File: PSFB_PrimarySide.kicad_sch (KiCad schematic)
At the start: 15 parts

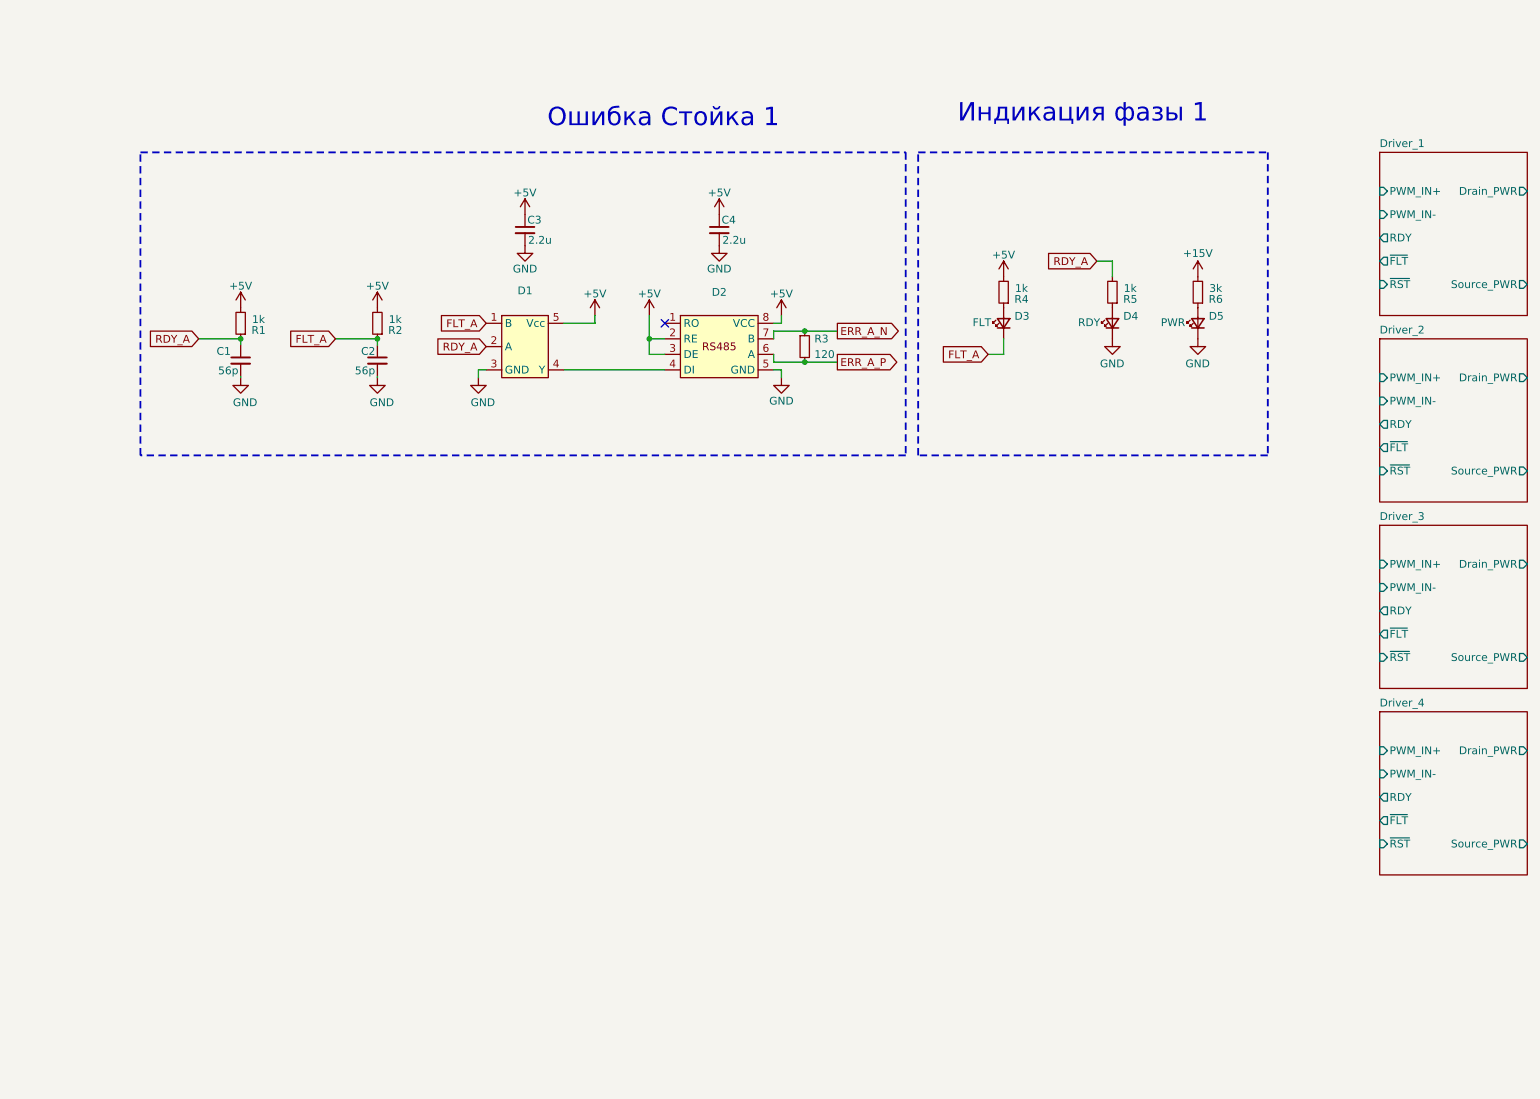
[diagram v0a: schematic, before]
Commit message: VER1.0: развел 4 канала
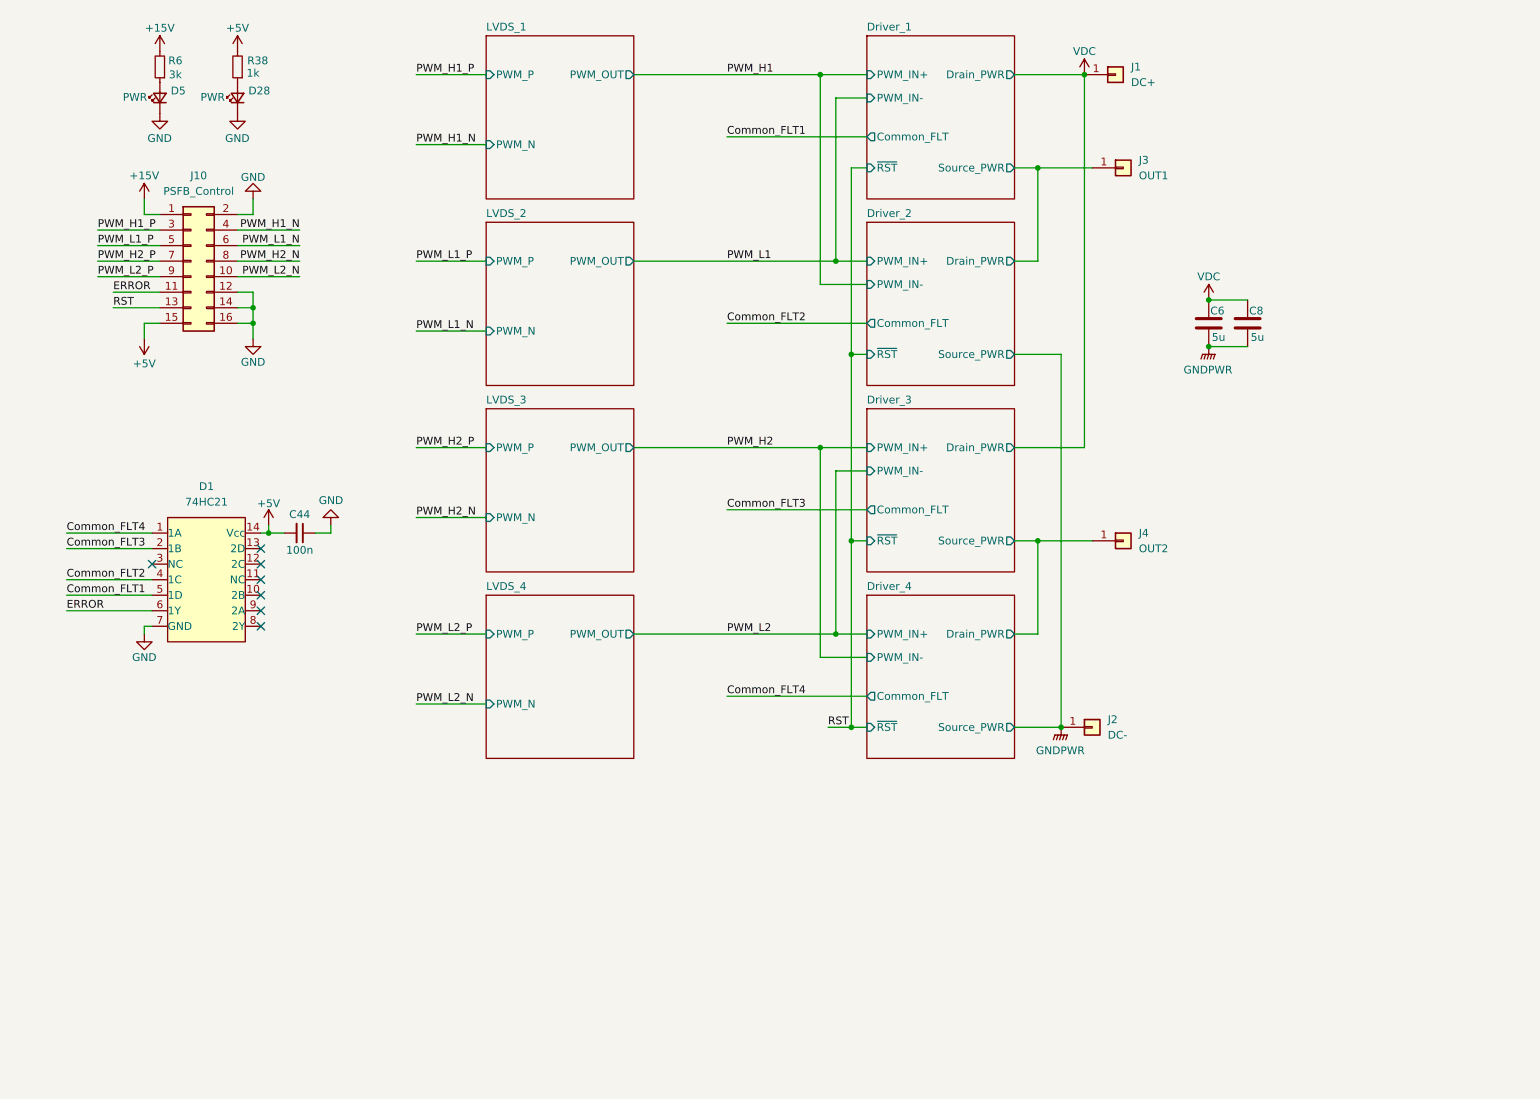
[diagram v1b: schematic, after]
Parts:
- removed C1, C2: 56p, Capacitor_SMD:C_0805_2012Metric_Pad1.18x1.45mm_HandSolder, symbol Device:C_Small
- removed C3, C4: 2.2u, Capacitor_SMD:C_0805_2012Metric_Pad1.18x1.45mm_HandSolder, symbol Device:C_Small
- removed D1: (no value), Package_TO_SOT_SMD:SOT-23-5_HandSoldering, symbol Logic_My:MC74VHC1GT08DTT1G
- removed D2: (no value), Package_SO:SOIC-8_3.9x4.9mm_P1.27mm, symbol Interface_My:ADM3485E_1
- removed D3, D4: (no value), LED_SMD:LED_0805_2012Metric_Pad1.15x1.40mm_HandSolder, symbol Device:LED_Small
- removed R1, R2, R4, R5: 1k, Resistor_SMD:R_0805_2012Metric_Pad1.20x1.40mm_HandSolder, symbol Device:R_Small
- removed R3: 120, Resistor_SMD:R_0805_2012Metric_Pad1.20x1.40mm_HandSolder, symbol Device:R_Small
- added C44: 100n, Capacitor_SMD:C_0805_2012Metric_Pad1.18x1.45mm_HandSolder, symbol Device:C_Small
- added C6, C8: 5u, Capacitor_THT:C_Rect_L31.5mm_W15.0mm_P27.50mm_MKS4, symbol Device:C
- added D1: 74HC21, Package_SO:SOIC-14_3.9x8.7mm_P1.27mm, symbol Logic_my:74HC21
- added D28: (no value), LED_SMD:LED_0805_2012Metric_Pad1.15x1.40mm_HandSolder, symbol Device:LED_Small
- added J1: DC+, symbol Connector_Generic:Conn_01x01
- added J10: PSFB_Control, Connector_IDC:IDC-Header_2x08_P2.54mm_Vertical, symbol Connector_Generic:Conn_02x08_Odd_Even
- added J2: DC-, symbol Connector_Generic:Conn_01x01
- added J3: OUT1, symbol Connector_Generic:Conn_01x01
- added J4: OUT2, symbol Connector_Generic:Conn_01x01
- added R38: 1k, Resistor_SMD:R_0805_2012Metric_Pad1.20x1.40mm_HandSolder, symbol Device:R_Small
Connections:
- net +15V: now also J10.1 (Pin_1)
- net +5V: now also C44.2, D1.14 (Vcc), J10.15 (Pin_15), R38.2
- net Driver_1/Source_PWR: now also J3.1 (Pin_1)
- net Driver_3/Source_PWR: now also J4.1 (Pin_1)
- net GND: now also C44.1, D1.7 (GND), D28.1 (K), J10.12 (Pin_12), J10.14 (Pin_14), J10.16 (Pin_16), J10.2 (Pin_2)
- new net: D28.2 (A), R38.1
- new net Common_FLT1: D1.5 (1D)
- new net Common_FLT2: D1.4 (1C)
- new net Common_FLT3: D1.2 (1B)
- new net Common_FLT4: D1.1 (1A)
- new net ERROR: D1.6 (1Y), J10.11 (Pin_11)
- new net GNDPWR: C6.2, C8.2, J2.1 (Pin_1)
- new net PWM_H1_N: J10.4 (Pin_4)
- new net PWM_H1_P: J10.3 (Pin_3)
- new net PWM_H2_N: J10.8 (Pin_8)
- new net PWM_H2_P: J10.7 (Pin_7)
- new net PWM_L1_N: J10.6 (Pin_6)
- new net PWM_L1_P: J10.5 (Pin_5)
- new net PWM_L2_N: J10.10 (Pin_10)
- new net PWM_L2_P: J10.9 (Pin_9)
- new net RST: J10.13 (Pin_13)
- new net VDC: C6.1, C8.1, J1.1 (Pin_1)
- no-connect marks 1 -> 7
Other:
- added sheet LVDS_1 (LVDS.kicad_sch)
- added sheet LVDS_2 (LVDS.kicad_sch)
- added sheet LVDS_3 (LVDS.kicad_sch)
- added sheet LVDS_4 (LVDS.kicad_sch)
- sheet Driver_1 ports: added Common_FLT; removed RDY, ~{FLT}
- sheet Driver_2 ports: added Common_FLT; removed RDY, ~{FLT}
- sheet Driver_3 ports: added Common_FLT; removed RDY, ~{FLT}
- sheet Driver_4 ports: added Common_FLT; removed RDY, ~{FLT}
- note removed: "Индикация фазы 1"
- note removed: "Ошибка Стойка 1"
- moved on the sheet: D5, R6

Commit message: VER1.0: добавил разъем под FFC
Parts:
- removed J10: PSFB_Control, Connector_IDC:IDC-Header_2x08_P2.54mm_Vertical, symbol Connector_Generic:Conn_02x08_Odd_Even
- added C14, C30: 100n, Capacitor_SMD:C_1812_4532Metric_Pad1.57x3.40mm_HandSolder, symbol Device:C
- added C3: 22u, Capacitor_Tantalum_SMD:CP_EIA-3216-18_Kemet-A_HandSolder, symbol Device:C_Polarized_Small
- added C49: 10u, Capacitor_Tantalum_SMD:CP_EIA-3216-18_Kemet-A_HandSolder, symbol Device:C_Polarized_Small
- added C50: 10u, Capacitor_SMD:C_1206_3216Metric_Pad1.33x1.80mm_HandSolder, symbol Device:C_Small
- added C53: 100n, Capacitor_SMD:C_0805_2012Metric_Pad1.18x1.45mm_HandSolder, symbol Device:C_Small
- added D2: K78xx-500R3, MORNSUN:K78xx-500R3 ÕýÊä³ö, symbol MORNSUN:K78xx-500R3 正输出
- added J10: PSFB_Control, Connector_FFC-FPC:Hirose_FH12-20S-0.5SH_1x20-1MP_P0.50mm_Horizontal, symbol Connector_Generic:Conn_01x20
- added J12, J9: Supply, Connector_PinSocket_2.54mm:PinSocket_2x02_P2.54mm_Vertical, symbol Connector_Generic:Conn_02x02_Odd_Even
- added U5: AMS1117-3.3, Package_TO_SOT_SMD:SOT-223-3_TabPin2, symbol Regulator_Linear:AMS1117-3.3
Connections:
- net +15V: now also C50.1, D2.1 (Vin), J10.1 (Pin_1), J10.2 (Pin_2), J9.2 (Pin_2), J9.4 (Pin_4)
- net +5V: now also C49.1, C53.1, D2.3 (+Vo), U5.3 (VI); no longer C44.2, D1.14 (Vcc), R38.2
- net ERROR: now also J10.6 (Pin_6)
- net GND: now also C3.2, C49.2, C50.2, C53.2, D2.2 (GND), J10.12 (Pin_12), J10.15 (Pin_15), J10.18 (Pin_18), J10.3 (Pin_3), J10.4 (Pin_4), J10.5 (Pin_5), J10.7 (Pin_7), J10.9 (Pin_9), J12.1 (Pin_1), J12.2 (Pin_2), J12.3 (Pin_3), J12.4 (Pin_4), J9.1 (Pin_1), J9.3 (Pin_3), U5.1 (GND)
- net GNDPWR: now also C14.2, C30.2
- net PWM_H1_N: now also J10.11 (Pin_11)
- net PWM_H1_P: now also J10.10 (Pin_10)
- net PWM_H2_N: now also J10.17 (Pin_17)
- net PWM_H2_P: now also J10.16 (Pin_16)
- net PWM_L1_N: now also J10.14 (Pin_14)
- net PWM_L1_P: now also J10.13 (Pin_13)
- net PWM_L2_N: now also J10.20 (Pin_20)
- net PWM_L2_P: now also J10.19 (Pin_19)
- net RST: now also J10.8 (Pin_8)
- net VDC: now also C14.1, C30.1
- new net +3.3V: C3.1, C44.2, D1.14 (Vcc), R38.2, U5.2 (VO)
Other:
- moved on the sheet: D28, D5, R38, R6

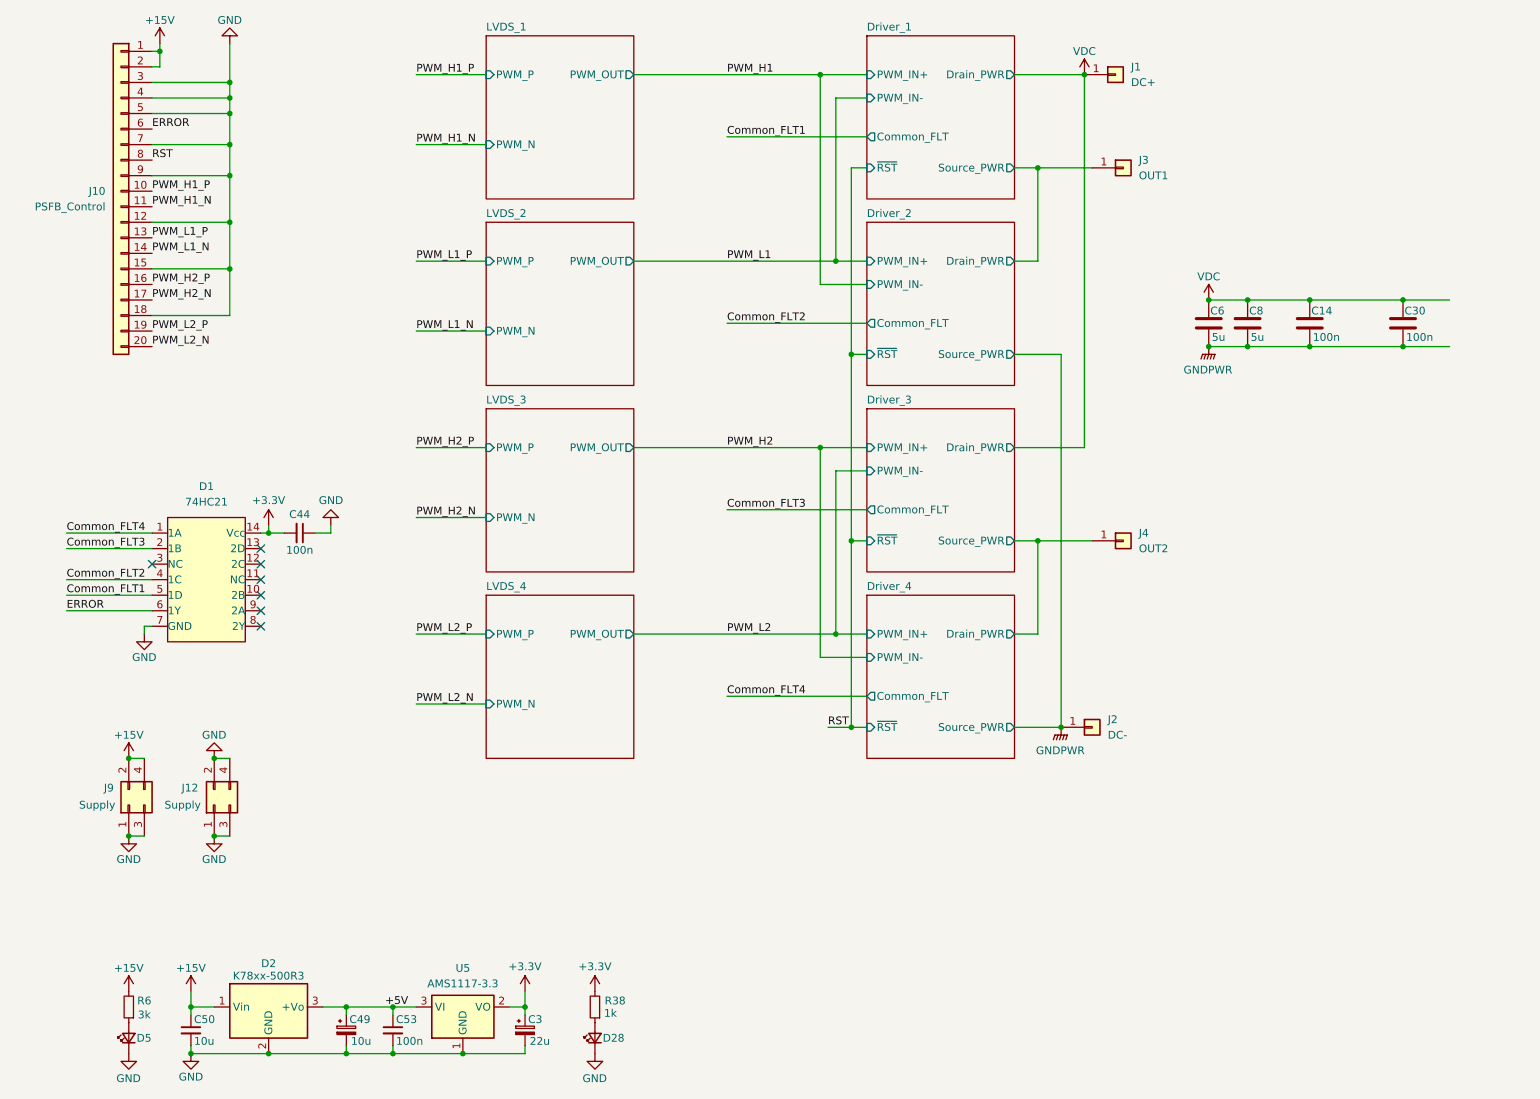
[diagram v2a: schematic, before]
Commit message: VER1.0: добавил плату питания драйверов и развел всю силовую плату
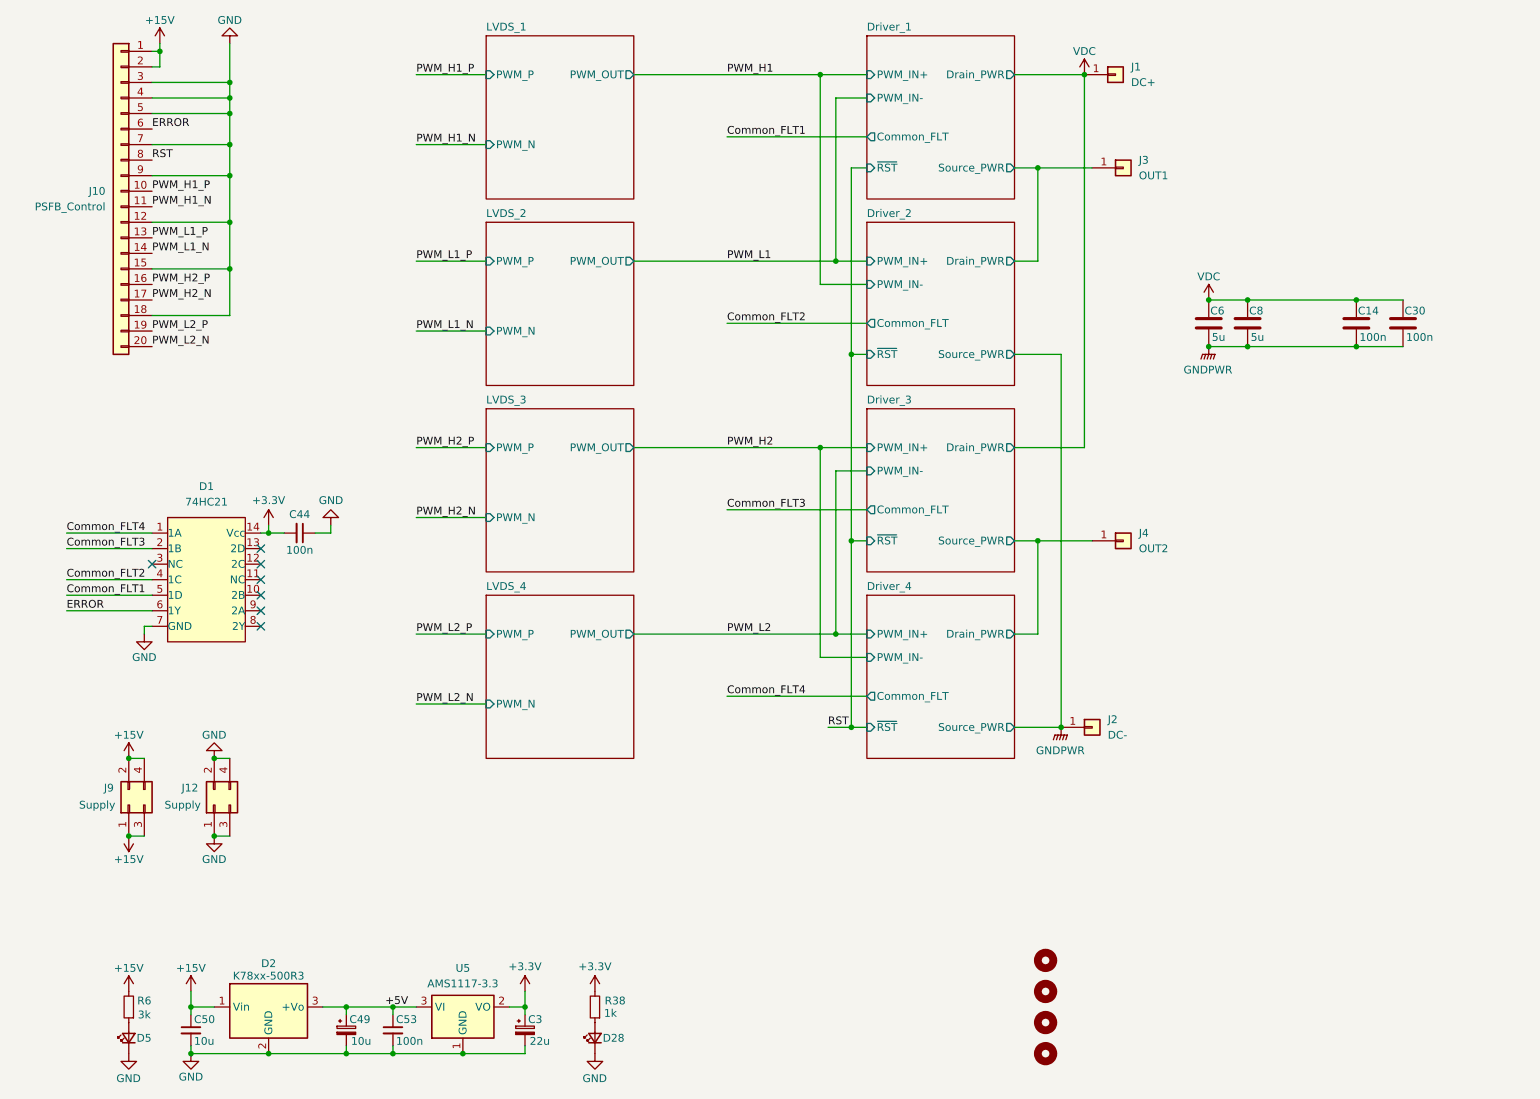
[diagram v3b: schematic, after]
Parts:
- added H1, H2, H3, H4: MountingHole, MountingHole:MountingHole_4.3mm_M4, symbol Mechanical:MountingHole
- J1, J2, J3, J4: footprint (none) -> Connector_my:Bush_1x8
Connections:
- net +15V: now also J9.1 (Pin_1), J9.3 (Pin_3)
- net GND: no longer J9.1 (Pin_1), J9.3 (Pin_3)
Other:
- moved on the sheet: C14

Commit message: VER1.0: добавил ресет общий
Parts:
- added Q5: (no value), Package_TO_SOT_SMD:SOT-23, symbol Device:Q_NPN_BEC
- added R100: 4.7k, Resistor_SMD:R_0805_2012Metric_Pad1.20x1.40mm_HandSolder, symbol Device:R_Small
- added R101: 1k, Resistor_SMD:R_0805_2012Metric_Pad1.20x1.40mm_HandSolder, symbol Device:R_Small
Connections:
- net +3.3V: now also R101.2
- net GND: now also Q5.2 (E)
- net RST: now also R100.1
- new net: Q5.1 (B), R100.2
- new net Driver_1/~{RST}: Q5.3 (C), R101.1

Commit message: VER1.0: сделал файлы для производства
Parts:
- C14, C30: Description P/N (none) -> Capacitor Film; Product Name (none) -> C1812X104K102T
- C3: Description P/N (none) -> Capacitor Tantalum SMD; Product Name (none) -> CA45-A010K226T
- C44, C50, C53: Description P/N Capacitor SMD 25+V -> Capacitor SMD 50V
- C49: Description P/N (none) -> Capacitor Tantalum SMD; Product Name (none) -> CA45-A010K106T
- C6, C8: Description P/N (none) -> Capacitor Film; Product Name (none) -> B32774D8505K000
- D1: value 74HC21 -> (none); Description P/N (none) -> AND; Product Name (none) -> 74HC21
- D2: value K78xx-500R3 -> (none); Description P/N (none) -> Linear regulator; Product Name (none) -> K7805-500R3
- D28, D5: Description P/N Yellow LED -> LEDs
- H1, H2, H3, H4: value MountingHole -> (none)
- J1, J2, J3, J4: now left out of the parts list
- J10: value PSFB_Control -> (none); Description P/N (none) -> Connector; Product Name (none) -> FH12-20S-0.5SH
- J12, J9: value Supply -> (none); Description P/N (none) -> Connector; Product Name (none) -> KLS1-208-2-04-S
- U5: value AMS1117-3.3 -> (none); Description P/N (none) -> Linear regulator; Product Name (none) -> AMS1117-3.3
